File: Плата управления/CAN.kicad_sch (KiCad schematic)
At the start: 4 parts, among them U3 ISO1050DUB

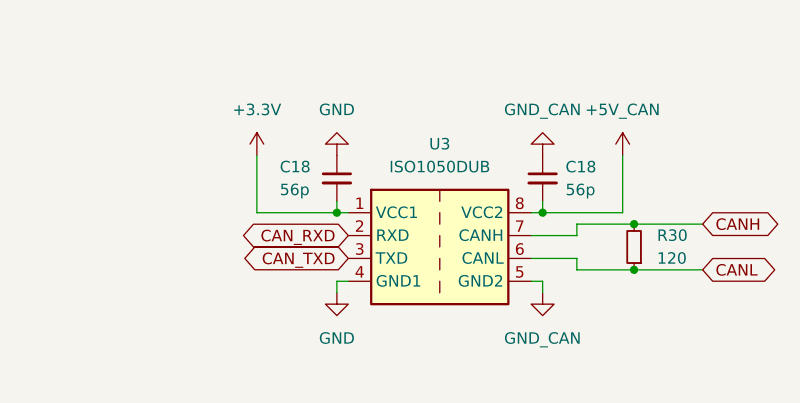
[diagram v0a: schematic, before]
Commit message: Добавил 3.3В CAN SN65HVD232
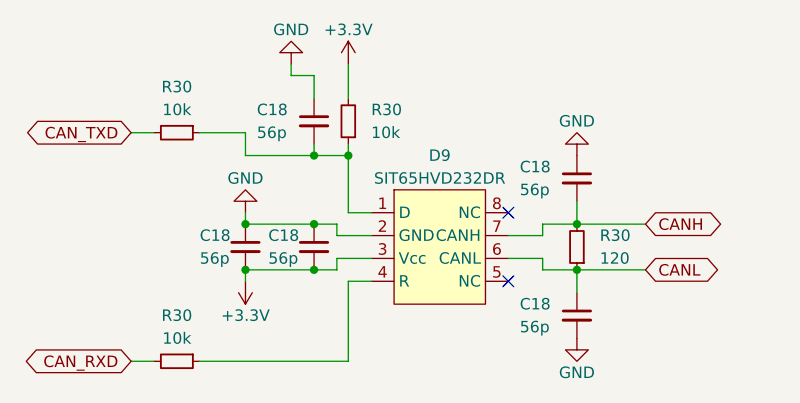
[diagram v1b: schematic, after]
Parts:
- removed C18 (x2): 56p, Capacitor_SMD:C_0603_1608Metric_Pad1.08x0.95mm_HandSolder, symbol Device:C_Small
- removed U3: ISO1050DUB, Package_SO:SOP-8_6.62x9.15mm_P2.54mm, symbol Interface_CAN_LIN:ISO1050DUB
- added C18 (x5): 56p, Capacitor_SMD:C_0603_1608Metric_Pad1.08x0.95mm_HandSolder, symbol Device:C_Small
- added D9: SIT65HVD232DR, Package_SO:SOIC-8_3.9x4.9mm_P1.27mm, symbol CAN_My:SIT65HVD232DR
- added R30 (x3): 10k, Resistor_SMD:R_0603_1608Metric_Pad0.98x0.95mm_HandSolder, symbol Device:R_Small
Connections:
- net +3.3V: now also C18.2, C18.2, D9.3 (Vcc), R30.2
- net CANH: now also C18.2, D9.7 (CANH)
- net CANL: now also C18.1, D9.6 (CANL)
- net CAN_RXD: now also R30.2
- net CAN_TXD: now also R30.2
- net GND: now also C18.1, C18.1, C18.1, C18.1, C18.2, D9.2 (GND)
- new net: C18.2, D9.1 (D), R30.1, R30.1
- new net: D9.4 (R), R30.1
- no-connect marks 0 -> 2
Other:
- moved on the sheet: R30

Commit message: Привел в порядок схему
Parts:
- renumbered D9 to D10
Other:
- note added: "CAN"
- moved on the sheet: C18, D10, R30
